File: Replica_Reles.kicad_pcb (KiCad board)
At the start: 2 copper layers, 60 x 145 mm, 70 parts, among them J1 Bornera, J2 Bornera, J3 Tira de Pines Macho, J4 Bornera, J5 Bornera, J6 Bornera, J7 Bornera, J8 Bornera, J9 Bornera, K1 SONGLE_SRD_Form_C, K2 SONGLE_SRD_Form_C, K3 SONGLE_SRD_Form_C, K4 SONGLE_SRD_Form_C, K5 SONGLE_SRD_Form_C, K6 SONGLE_SRD_Form_C, K7 SONGLE_SRD_Form_C, K8 SONGLE_SRD_Form_C, Q1 S8050, Q2 S8050, Q3 S8050, Q4 S8050, Q5 S8050, Q6 S8050, Q7 S8050, Q8 S8050, U1 PC817, U2 PC817, U3 PC817, U4 PC817, U5 PC817, U6 PC817, U7 PC817, U8 PC817

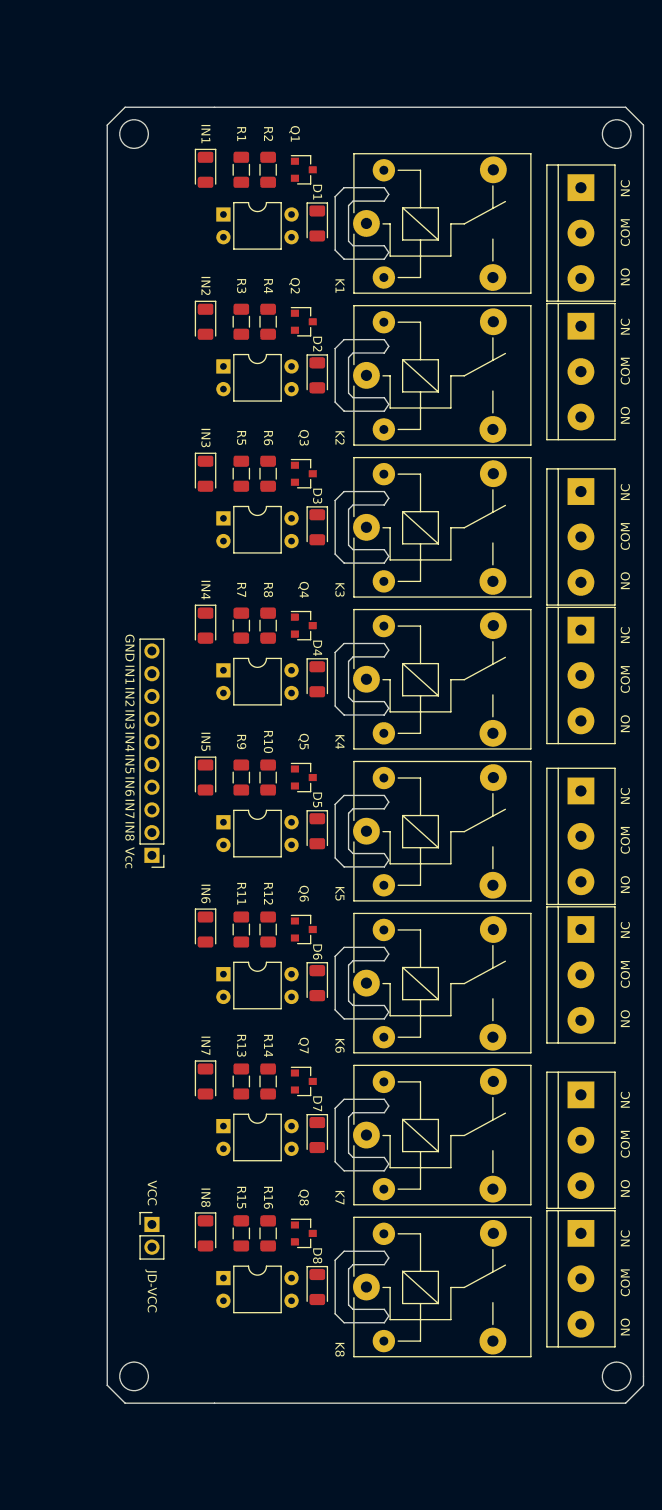
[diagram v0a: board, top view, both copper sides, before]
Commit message: Cambios en posicionamiento, ruteo y mas documentacion
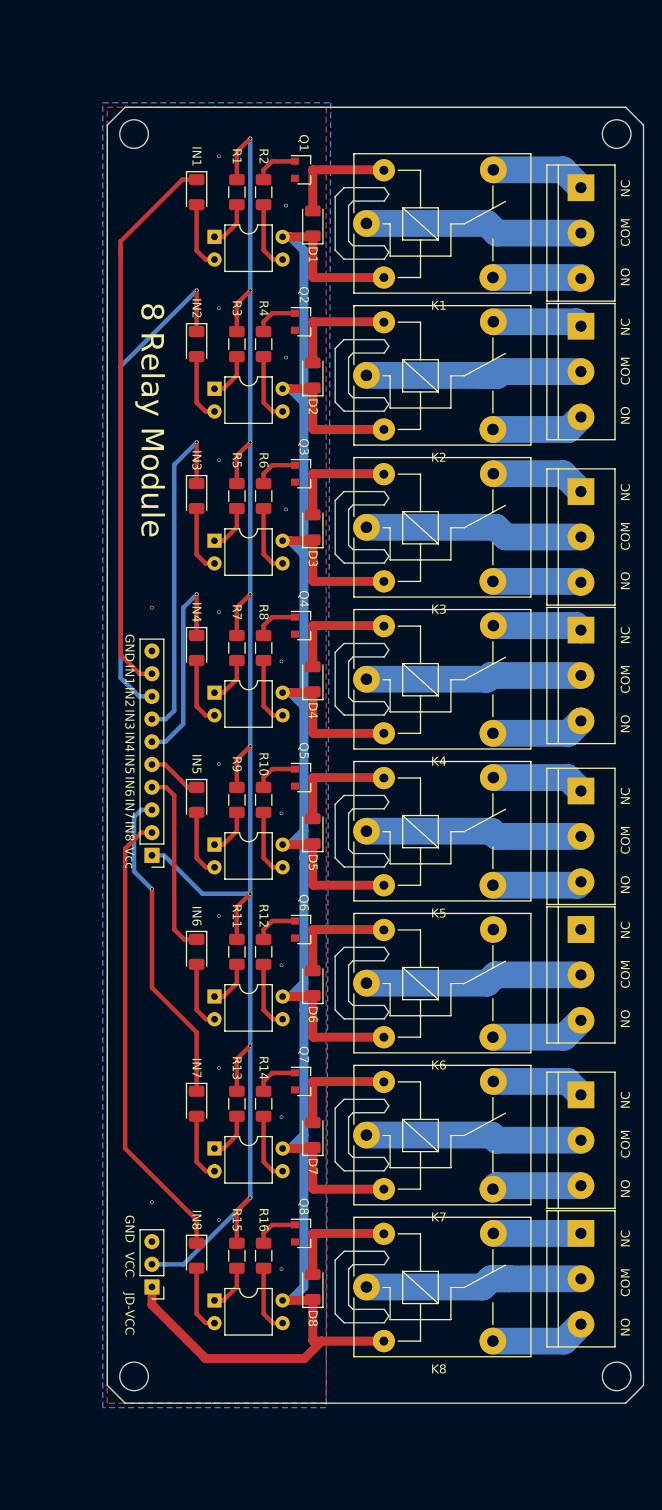
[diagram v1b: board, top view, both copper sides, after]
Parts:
- removed JP1: VCC JD-VCC, Connector_PinHeader_2.54mm:PinHeader_1x02_P2.54mm_Vertical
- added J10: Conn_01x03, Connector_PinHeader_2.54mm:PinHeader_1x03_P2.54mm_Vertical, F.Cu at (45.0, 162.0)
- K1, K2, K3, K4, K5, K6, K7, K8: footprint Relay_THT:Relay_SPDT_SANYOU_SRD_Series_Form_C -> Relay_THT:Relay_SPDT_SONGLE_SRD_Series_Form_C
- moved IN1 2.69 mm to (50.0, 39.5)
- moved IN2 2.69 mm to (50.0, 56.5)
- moved IN3 2.69 mm to (50.0, 73.5)
- moved IN4 2.69 mm to (50.0, 90.5)
- moved IN5 2.69 mm to (50.0, 107.5)
- moved IN6 2.69 mm to (50.0, 124.5)
- moved IN7 2.69 mm to (50.0, 141.5)
- moved IN8 2.69 mm to (50.0, 158.5)
- moved U1 2.69 mm to (52.0, 44.5)
- moved U2 2.69 mm to (52.0, 61.5)
- moved U3 2.69 mm to (52.0, 78.5)
- moved U4 2.69 mm to (52.0, 95.5)
- moved U5 2.69 mm to (52.0, 112.5)
- moved U6 2.69 mm to (52.0, 129.5)
- moved U7 2.69 mm to (52.0, 146.5)
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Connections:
- Q1 pad 1: GND -> Net-(Q1-Pad1)
- Q1 pad 2: Net-(Q1-Pad2) -> GND
- Q2 pad 1: GND -> Net-(Q2-Pad1)
- Q2 pad 2: Net-(Q2-Pad2) -> GND
- Q3 pad 1: GND -> Net-(Q3-Pad1)
- Q3 pad 2: Net-(Q3-Pad2) -> GND
- Q4 pad 1: GND -> Net-(Q4-Pad1)
- Q4 pad 2: Net-(Q4-Pad2) -> GND
- Q5 pad 1: GND -> Net-(Q5-Pad1)
- Q5 pad 2: Net-(Q5-Pad2) -> GND
- Q6 pad 1: GND -> Net-(Q6-Pad1)
- Q6 pad 2: Net-(Q6-Pad2) -> GND
- Q7 pad 1: GND -> Net-(Q7-Pad1)
- Q7 pad 2: Net-(Q7-Pad2) -> GND
- Q8 pad 1: GND -> Net-(Q8-Pad1)
- Q8 pad 2: Net-(Q8-Pad2) -> GND
- R10 pad 1: Net-(Q5-Pad2) -> Net-(Q5-Pad1)
- R12 pad 1: Net-(Q6-Pad2) -> Net-(Q6-Pad1)
- R14 pad 1: Net-(Q7-Pad2) -> Net-(Q7-Pad1)
- R16 pad 1: Net-(Q8-Pad2) -> Net-(Q8-Pad1)
- R2 pad 1: Net-(Q1-Pad2) -> Net-(Q1-Pad1)
- R4 pad 1: Net-(Q2-Pad2) -> Net-(Q2-Pad1)
- R6 pad 1: Net-(Q3-Pad2) -> Net-(Q3-Pad1)
- R8 pad 1: Net-(Q4-Pad2) -> Net-(Q4-Pad1)
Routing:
- net /JD-VCC: track 0.00 -> 292.2 mm
- net +5V: track 0.00 -> 188.6 mm, vias 0 -> 8
- net /IN1: track 0.00 -> 63.4 mm
- net /IN2: track 0.00 -> 55.8 mm, vias 0 -> 1
- net /IN8: track 0.00 -> 51.2 mm
- net /IN3: track 0.00 -> 38.5 mm, vias 0 -> 1
- net /IN7: track 0.00 -> 35.9 mm, vias 0 -> 1
- net Net-(J9-Pad2): track 0.00 -> 26.2 mm
- net Net-(J2-Pad2): track 0.00 -> 25.6 mm
- net Net-(J4-Pad2): track 0.00 -> 24.4 mm
- net Net-(J1-Pad2): track 0.00 -> 24.4 mm
- net Net-(J7-Pad2): track 0.00 -> 24.3 mm
- net Net-(J5-Pad2): track 0.00 -> 24.3 mm
- net Net-(J8-Pad2): track 0.00 -> 24.2 mm
- net Net-(J6-Pad2): track 0.00 -> 24.2 mm
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- added copper zone on B.Cu, net GND
- added copper zone on F.Cu, net GND
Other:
- net class Default: clearance 0.2 -> 0.5; trace_width 0.25 -> 0.5; via_dia 0.8 -> 0.4; via_drill 0.4 -> 0.3
- rule trace_clearance: 0.2 -> 0.5
- rule trace_min: 0.2 -> 0.5
- board text added: "8 Relay Module"

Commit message: Arreglos menores y agregado de documentacion
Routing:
- net +5V: track 188.6 -> 228.1 mm
- net Net-(J7-Pad1): track 0.00 -> 9.80 mm
- net /IN4: track 24.0 -> 30.6 mm
- net /IN2: track 55.8 -> 52.4 mm
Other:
- net class Default: via_dia 0.4 -> 0.6; via_drill 0.3 -> 0.5
- board text added: "Minimos (Replica modulo 4 reles propio - Ver documentacion) Grillas 1mm, 0.5 mm Vias 0.6 / 0.5 Margen 0.5mm Pistas 0.5mm, 1mm, 3mm Terminacion HASL"

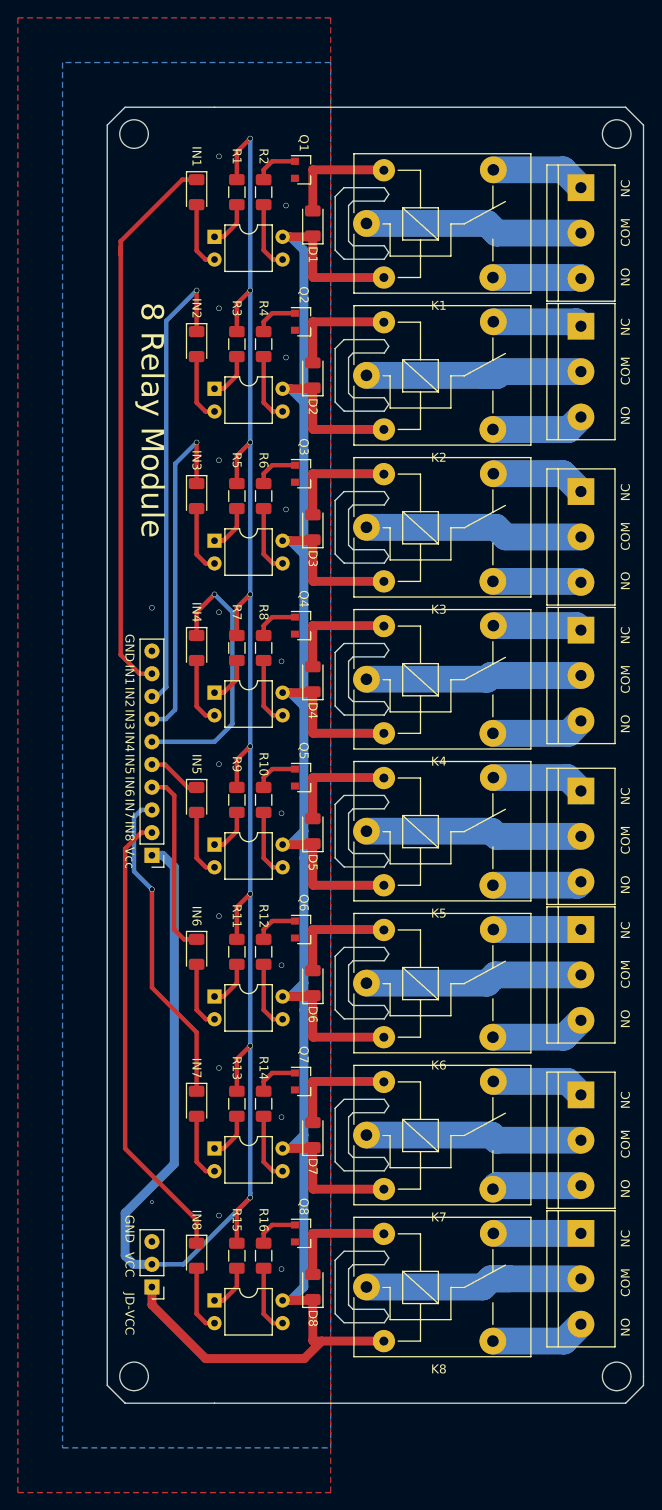
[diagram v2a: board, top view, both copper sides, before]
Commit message: Agregado fiduciales, texto en capa de cobre y arreglo de errores
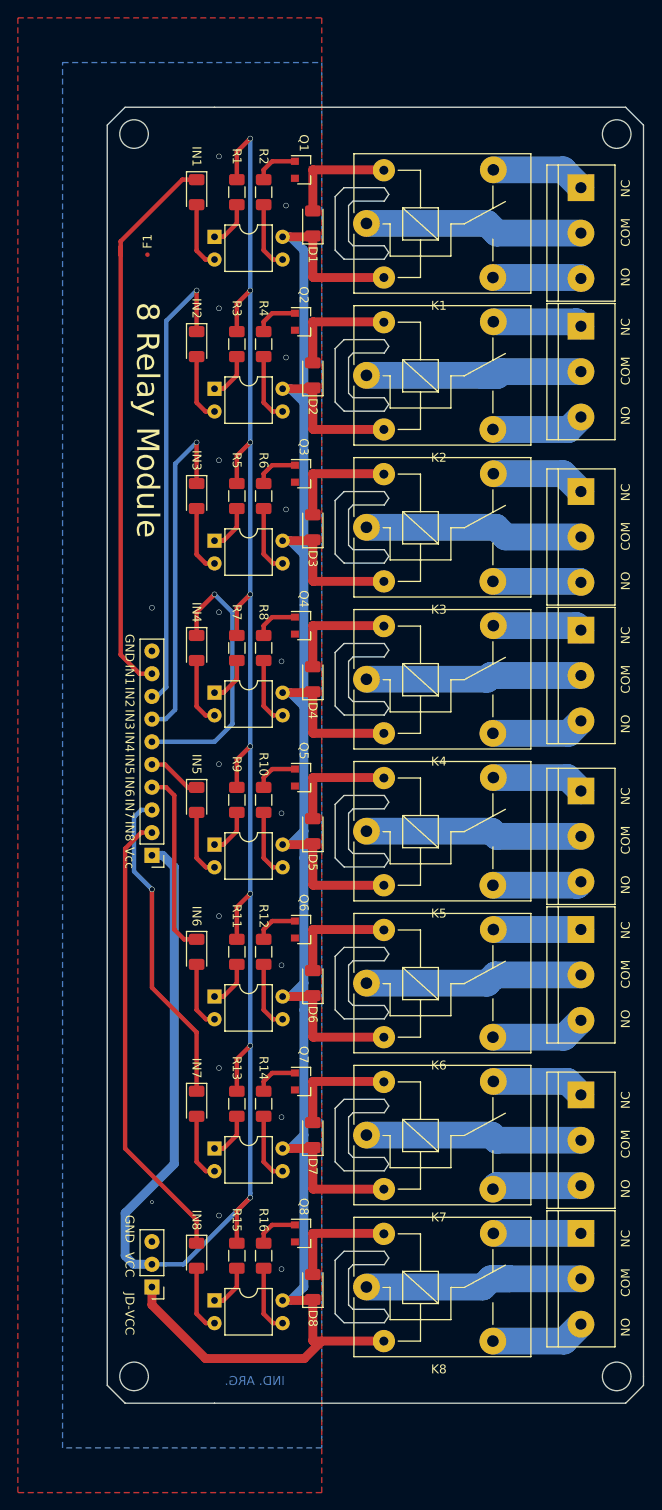
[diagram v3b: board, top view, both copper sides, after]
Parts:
- added F1: Fiducial, Fiducial:Fiducial_0.5mm_Dia_1mm_Outer, F.Cu at (44.5, 46.5)
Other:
- board text added: "IND. ARG."
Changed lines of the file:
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@@
   (general
     (thickness 1.6)
-    (drawings 164)
+    (drawings 165)
     (tracks 358)
     (zones 0)
-    (modules 70)
+    (modules 71)
     (nets 76)
   )
@@
   )
   (setup
-    (last_trace_width 1)
+    (last_trace_width 0.5)
     (user_trace_width 0.5)
     (user_trace_width 1)
@@
     )
   )
+  (module Fiducial:Fiducial_0.5mm_Dia_1mm_Outer (layer F.Cu)
+    (at 44.5 46.5)
+    (descr "Circular Fiducial, 0.5mm bare copper top; 1mm keepout (Level C)")
+    (tags marker)
+    (attr virtual)
+    (fp_text reference F1 (at 0 -1.5 -90) (layer F.SilkS)
+      (effects (font (size 1 1) (thickness 0.15)))
+    )
+    (fp_text value Fiducial (at 0 1.5) (layer F.Fab)
+      (effects (font (size 1 1) (thickness 0.15)))
+    )
+    (fp_circle (center 0 0) (end 0.5 0) (layer F.Fab) (width 0.1))
+    (fp_text user %R (at 0 0) (layer F.Fab)
+      (effects (font (size 0.2 0.2) (thickness 0.04)))
+    )
+    (fp_circle (center 0 0) (end 0.75 0) (layer F.CrtYd) (width 0.05))
+    (pad ~ smd circle (at 0 0) (size 0.5 0.5) (layers F.Cu F.Mask)
+      (solder_mask_margin 0.25) (clearance 0.25))
+  )
+  (gr_text "IND. ARG." (at 56.5 172.5) (layer B.Cu)
+    (effects (font (size 1 1) (thickness 0.25)) (justify mirror))
+  )
   (dimension 60 (width 0.3) (layer Dwgs.User)
     (gr_text "60.000 mm" (at 70 16.9) (layer Dwgs.User)
@@
     (effects (font (size 1.5 1.5) (thickness 0.3)))
   )
-  (gr_text "8 Relay Module" (at 45 65 270) (layer F.SilkS)
+  (gr_text "8 Relay Module" (at 44.5 65 270) (layer F.SilkS)
     (effects (font (size 2.5 2.5) (thickness 0.4)))
   )
@@
   (segment (start 58.45 155.05) (end 57.5 156) (width 0.5) (layer F.Cu) (net 75))
   (segment (start 57.5 156) (end 57.5 157.1) (width 0.5) (layer F.Cu) (net 75))
-  (zone (net 19) (net_name GND) (layer B.Cu) (hatch edge 0.508)
+  (zone (net 0) (net_name "") (layer B.Mask) (hatch edge 0.508)
     (connect_pads (clearance 0.3))
-    (min_thickness 0.3)
-    (fill yes (arc_segments 16) (thermal_gap 0.5) (thermal_bridge_width 0.5))
+    (min_thickness 0.254)
+    (fill yes (arc_segments 16) (thermal_gap 0.508) (thermal_bridge_width 0.508))
     (polygon
       (pts
-        (xy 35 25) (xy 35 180) (xy 65 180) (xy 65 25)
+        (xy 52.5 171.5) (xy 52.5 173.5) (xy 60.5 173.5) (xy 60.5 171.5)
       )
     )
@@
     (polygon
       (pts
-        (xy 30 20) (xy 30 185) (xy 65 185) (xy 65 20)
+        (xy 30 20) (xy 64 20) (xy 64 185) (xy 30 185)
+      )
+    )
+  )
+  (zone (net 19) (net_name GND) (layer B.Cu) (hatch edge 0.508)
+    (connect_pads (clearance 0.3))
+    (min_thickness 0.2)
+    (fill yes (arc_segments 16) (thermal_gap 0.5) (thermal_bridge_width 0.5))
+    (polygon
+      (pts
+        (xy 35 25) (xy 64 25) (xy 64 180) (xy 35 180)
       )
     )

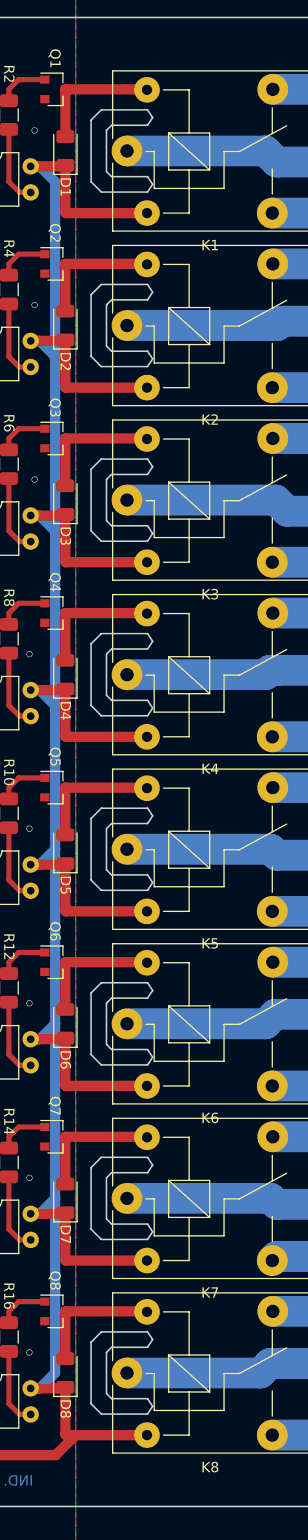
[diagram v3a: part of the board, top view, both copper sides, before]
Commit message: Arreglos de revision - Problema persistente: No es posible visualizar huella propia de los reles
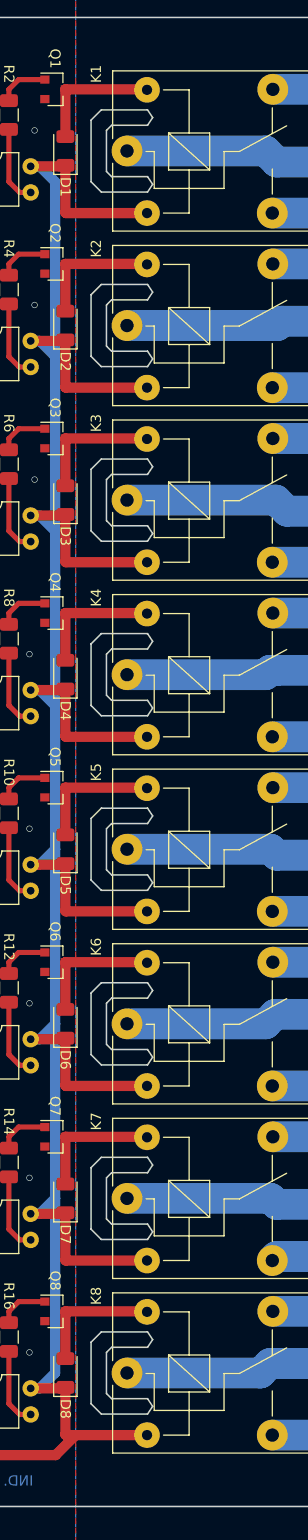
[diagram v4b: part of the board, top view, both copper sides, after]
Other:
- board text added: "Minimos (Replica modulo 4 reles propio - Ver documentacion) Grillas 1mm, 0.5 mm Vias 0.6mm / 0.5mm Agujero minimo 0.75mm Margen 0.5mm Distancia al borde minima: 1.25mm Pistas 0.5mm, 1mm, 3mm Terminacion HASL"
- board text removed: "Minimos (Replica modulo 4 reles propio - Ver documentacion) Grillas 1mm, 0.5 mm Vias 0.6 / 0.5 Margen 0.5mm Pistas 0.5mm, 1mm, 3mm Terminacion HASL"
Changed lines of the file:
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@@
     (descr "relay Sanyou SRD series Form C http://www.sanyourelay.ca/public/products/pdf/SRD.pdf")
     (tags "relay Sanyu SRD form C")
-    (fp_text reference K1 (at 8.1 9.2) (layer F.SilkS)
+    (fp_text reference K1 (at -3 -7.5 -90) (layer F.SilkS)
       (effects (font (size 1 1) (thickness 0.15)))
     )
@@
     (descr "relay Sanyou SRD series Form C http://www.sanyourelay.ca/public/products/pdf/SRD.pdf")
     (tags "relay Sanyu SRD form C")
-    (fp_text reference K2 (at 8.1 9.2) (layer F.SilkS)
+    (fp_text reference K2 (at -3 -7.5 -90) (layer F.SilkS)
       (effects (font (size 1 1) (thickness 0.15)))
     )
@@
     (descr "relay Sanyou SRD series Form C http://www.sanyourelay.ca/public/products/pdf/SRD.pdf")
     (tags "relay Sanyu SRD form C")
-    (fp_text reference K3 (at 8.1 9.2) (layer F.SilkS)
+    (fp_text reference K3 (at -3 -7.5 -90) (layer F.SilkS)
       (effects (font (size 1 1) (thickness 0.15)))
     )
@@
     (descr "relay Sanyou SRD series Form C http://www.sanyourelay.ca/public/products/pdf/SRD.pdf")
     (tags "relay Sanyu SRD form C")
-    (fp_text reference K4 (at 8.1 9.2) (layer F.SilkS)
+    (fp_text reference K4 (at -3 -7.5 -90) (layer F.SilkS)
       (effects (font (size 1 1) (thickness 0.15)))
     )
@@
     (descr "relay Sanyou SRD series Form C http://www.sanyourelay.ca/public/products/pdf/SRD.pdf")
     (tags "relay Sanyu SRD form C")
-    (fp_text reference K5 (at 8.1 9.2) (layer F.SilkS)
+    (fp_text reference K5 (at -3 -7.5 -90) (layer F.SilkS)
       (effects (font (size 1 1) (thickness 0.15)))
     )
@@
     (descr "relay Sanyou SRD series Form C http://www.sanyourelay.ca/public/products/pdf/SRD.pdf")
     (tags "relay Sanyu SRD form C")
-    (fp_text reference K6 (at 8.1 9.2) (layer F.SilkS)
+    (fp_text reference K6 (at -3 -7.5 -90) (layer F.SilkS)
       (effects (font (size 1 1) (thickness 0.15)))
     )
@@
     (descr "relay Sanyou SRD series Form C http://www.sanyourelay.ca/public/products/pdf/SRD.pdf")
     (tags "relay Sanyu SRD form C")
-    (fp_text reference K7 (at 8.1 9.2) (layer F.SilkS)
+    (fp_text reference K7 (at -3 -7.5 -90) (layer F.SilkS)
       (effects (font (size 1 1) (thickness 0.15)))
     )
@@
     (descr "relay Sanyou SRD series Form C http://www.sanyourelay.ca/public/products/pdf/SRD.pdf")
     (tags "relay Sanyu SRD form C")
-    (fp_text reference K8 (at 8.1 9.2) (layer F.SilkS)
+    (fp_text reference K8 (at -3 -7.5 -90) (layer F.SilkS)
       (effects (font (size 1 1) (thickness 0.15)))
     )
@@
     (arrow2b (pts (xy 40 19) (xy 41.126504 18.413579)))
   )
-  (gr_text "Minimos (Replica modulo 4 reles propio - Ver documentacion)\nGrillas 1mm, 0.5 mm\nVias 0.6  / 0.5\nMargen 0.5mm\nPistas 0.5mm, 1mm, 3mm\nTerminacion HASL\n" (at 152.5 98.5) (layer Dwgs.User)
+  (gr_text "Minimos (Replica modulo 4 reles propio - Ver documentacion)\nGrillas 1mm, 0.5 mm\nVias 0.6mm / 0.5mm\nAgujero minimo 0.75mm\nMargen 0.5mm\nDistancia al borde minima: 1.25mm\nPistas 0.5mm, 1mm, 3mm\nTerminacion HASL\n" (at 152.5 98.5) (layer Dwgs.User)
     (effects (font (size 1.5 1.5) (thickness 0.3)))
   )

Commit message: Error footprint propio solucionado
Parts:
- J10: value Conn_01x03 -> Tira de Pines Macho
- K1, K2, K3, K4, K5, K6, K7, K8: footprint Relay_THT:Relay_SPDT_SONGLE_SRD_Series_Form_C -> SONGLE_THT:Relay_SPDT_SONGLE_SRD_Series_Form_C

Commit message: Arreglos luego de la revision del profesor
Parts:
- added F2: Fiducial, Fiducial:Fiducial_0.5mm_Dia_1mm_Outer, F.Cu at (92.0, 33.0)
- added F3: Fiducial, Fiducial:Fiducial_0.5mm_Dia_1mm_Outer, F.Cu at (48.0, 172.5)
- added REF**: OSHW-Logo2_7.3x6mm_SilkScreen, Symbol:OSHW-Logo2_7.3x6mm_SilkScreen, F.Cu at (44.5, 42.5)
- moved F1 13.9 mm to (48.0, 33.0)
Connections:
- net /JD-VCC renamed VCC
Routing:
- net GND: vias 18 -> 0
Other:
- net class Default: via_dia 0.6 -> 2
- board text added: "8 Relay Module V1.2"
- board text added: "Minimos en concordancia con Ernesto Mayer S.A. Grillas 1mm, 0.5 mm Vias 2mm / 0.5mm Agujero minimo 0.5mm Margen 0.5mm Distancia al borde minima: 1.25mm Pistas 0.5mm, 1mm, 3mm Terminacion HASL"
- board text removed: "8 Relay Module"
- board text removed: "Minimos (Replica modulo 4 reles propio - Ver documentacion) Grillas 1mm, 0.5 mm Vias 0.6mm / 0.5mm Agujero minimo 0.75mm Margen 0.5mm Distancia al borde minima: 1.25mm Pistas 0.5mm, 1mm, 3mm Terminacion HASL"
